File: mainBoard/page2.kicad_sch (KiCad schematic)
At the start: 4 parts, among them IC1 TCAN3414DR, J12 Conn_02x20_Odd_Even, J13 RJ45

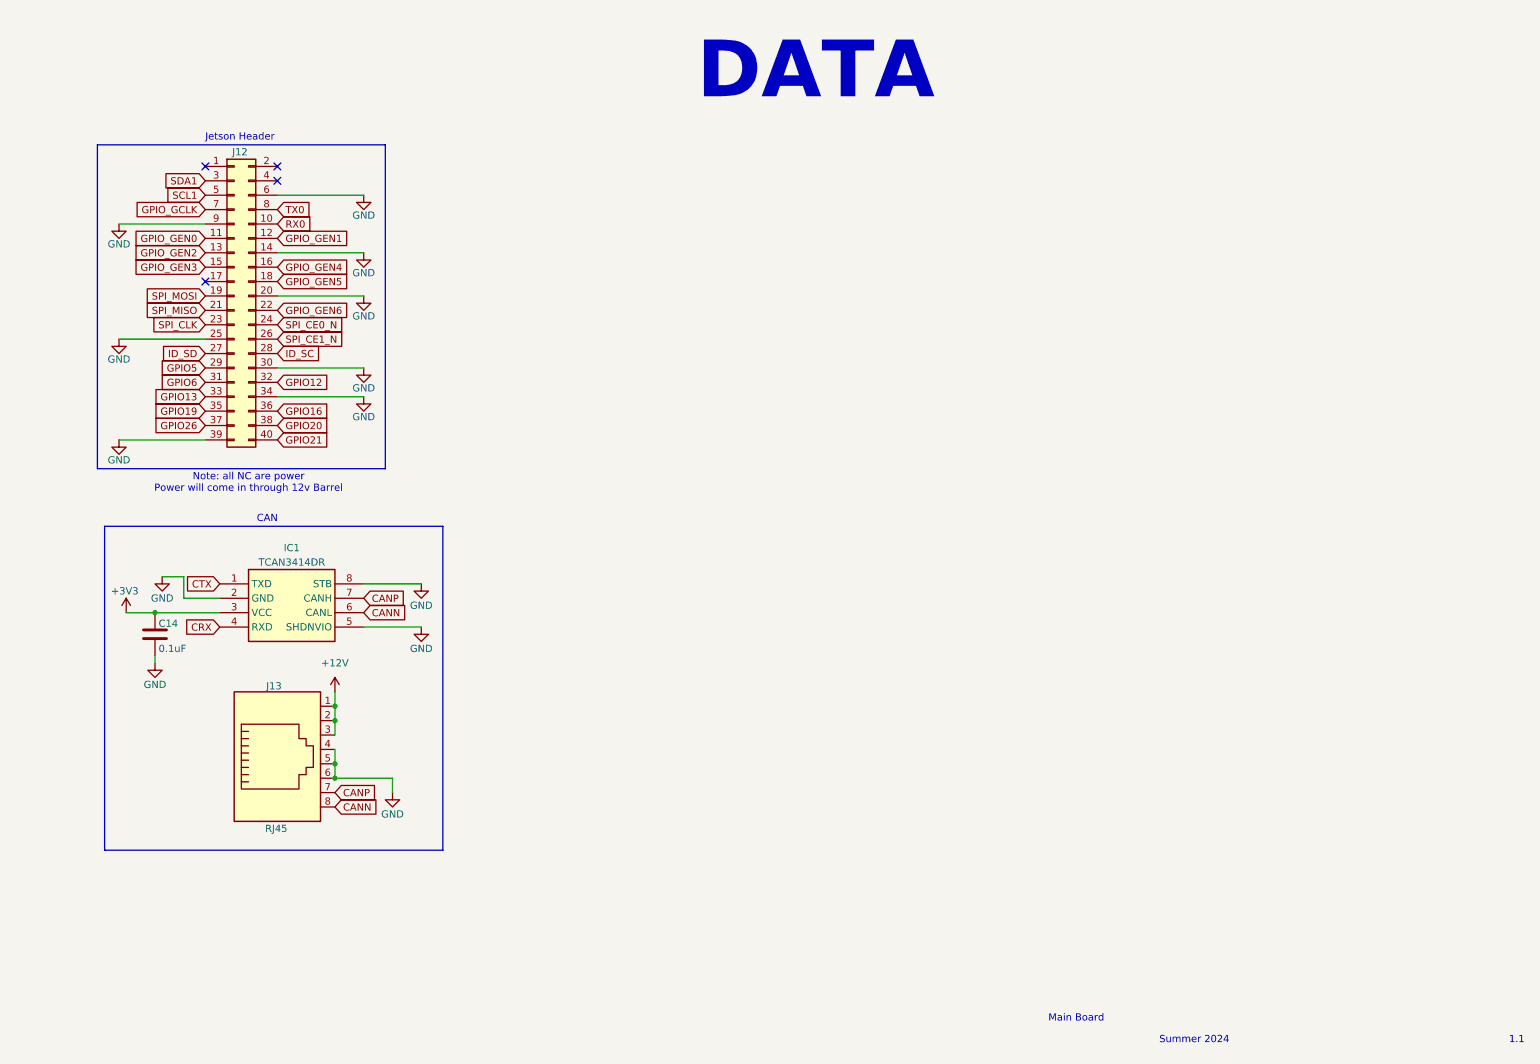
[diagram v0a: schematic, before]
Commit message: Added QWIIC Connectors for i2c, ethernet ports for attachment, updated XT style power connector counts, added i2c multiplexer
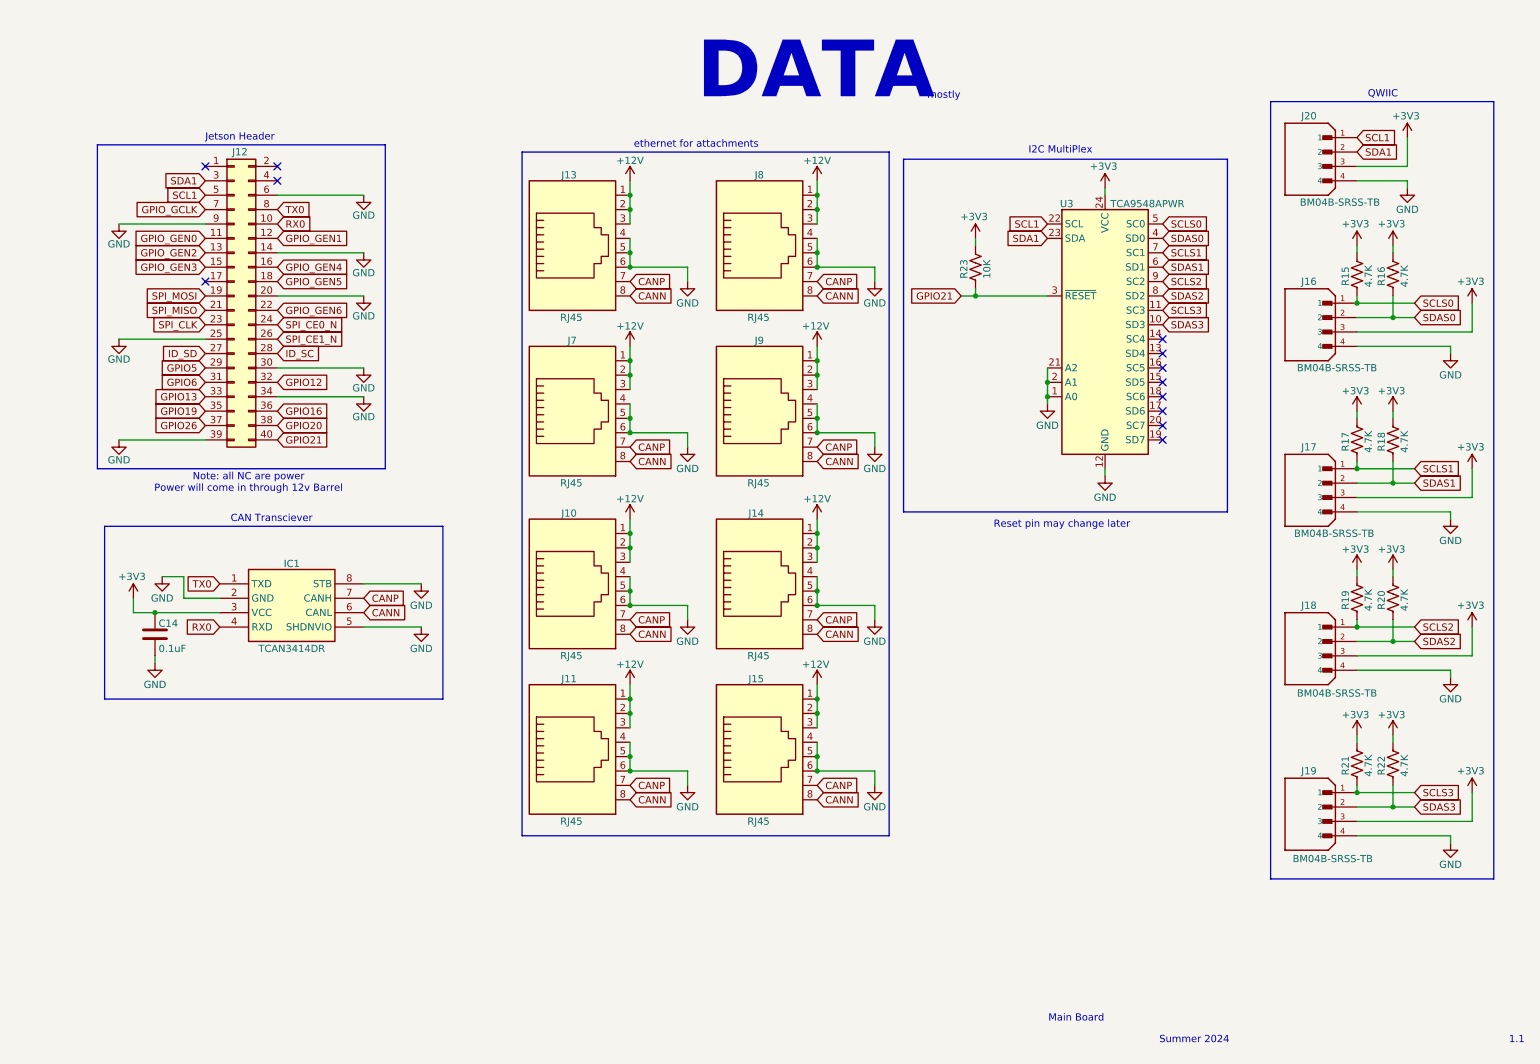
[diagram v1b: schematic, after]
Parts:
- added J10, J11, J14, J15, J7, J8, J9: RJ45, symbol Connector:RJ45
- added J16, J17, J18, J19, J20: BM04B-SRSS-TB, Connector_JST:JST_SH_BM04B-SRSS-TB_1x04-1MP_P1.00mm_Vertical, symbol QWIIC:PRT-14417
- added R15, R16, R17, R18, R19, R20, R21, R22: 4.7K, Resistor_SMD:R_0805_2012Metric_Pad1.20x1.40mm_HandSolder, symbol Device:R_US
- added R23: 10K, Resistor_SMD:R_0805_2012Metric_Pad1.20x1.40mm_HandSolder, symbol Device:R_US
- added U3: TCA9548APWR, Package_SO:TSSOP-24_4.4x7.8mm_P0.65mm, symbol Interface_Expansion:TCA9548APWR
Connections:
- net CRX is gone; now on net RX0: IC1.4 (RXD)
- net CTX is gone; now on net TX0: IC1.1 (TXD)
- net +12V: now also J10.1, J10.2, J10.3, J11.1, J11.2, J11.3, J14.1, J14.2, J14.3, J15.1, J15.2, J15.3, J7.1, J7.2, J7.3, J8.1, J8.2, J8.3, J9.1, J9.2, J9.3
- net +3V3: now also J16.3, J17.3, J18.3, J19.3, J20.3, R15.1, R16.1, R17.1, R18.1, R19.1, R20.1, R21.1, R22.1, R23.1, U3.24 (VCC)
- net CANN: now also J10.8, J11.8, J14.8, J15.8, J7.8, J8.8, J9.8
- net CANP: now also J10.7, J11.7, J14.7, J15.7, J7.7, J8.7, J9.7
- net GND: now also J10.4, J10.5, J10.6, J11.4, J11.5, J11.6, J14.4, J14.5, J14.6, J15.4, J15.5, J15.6, J16.4, J17.4, J18.4, J19.4, J20.4, J7.4, J7.5, J7.6, J8.4, J8.5, J8.6, J9.4, J9.5, J9.6, U3.1 (A0), U3.12 (GND), U3.2 (A1), U3.21 (A2)
- net GPIO21: now also R23.2, U3.3 (~{RESET})
- net SCL1: now also J20.1, U3.22 (SCL)
- net SDA1: now also J20.2, U3.23 (SDA)
- new net SCLS0: J16.1, R15.2, U3.5 (SC0)
- new net SCLS1: J17.1, R17.2, U3.7 (SC1)
- new net SCLS2: J18.1, R19.2, U3.9 (SC2)
- new net SCLS3: J19.1, R21.2, U3.11 (SC3)
- new net SDAS0: J16.2, R16.2, U3.4 (SD0)
- new net SDAS1: J17.2, R18.2, U3.6 (SD1)
- new net SDAS2: J18.2, R20.2, U3.8 (SD2)
- new net SDAS3: J19.2, R22.2, U3.10 (SD3)
- no-connect marks 4 -> 12
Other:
- note added: "CAN Transciever"
- note added: "I2C MultiPlex"
- note added: "QWIIC"
- note added: "Reset pin may change later"
- note added: "ethernet for attachments"
- note added: "mostly"
- note removed: "CAN"
- moved on the sheet: J13

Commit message: Minor changes, renamed ethernet ports to attachment and adding warning
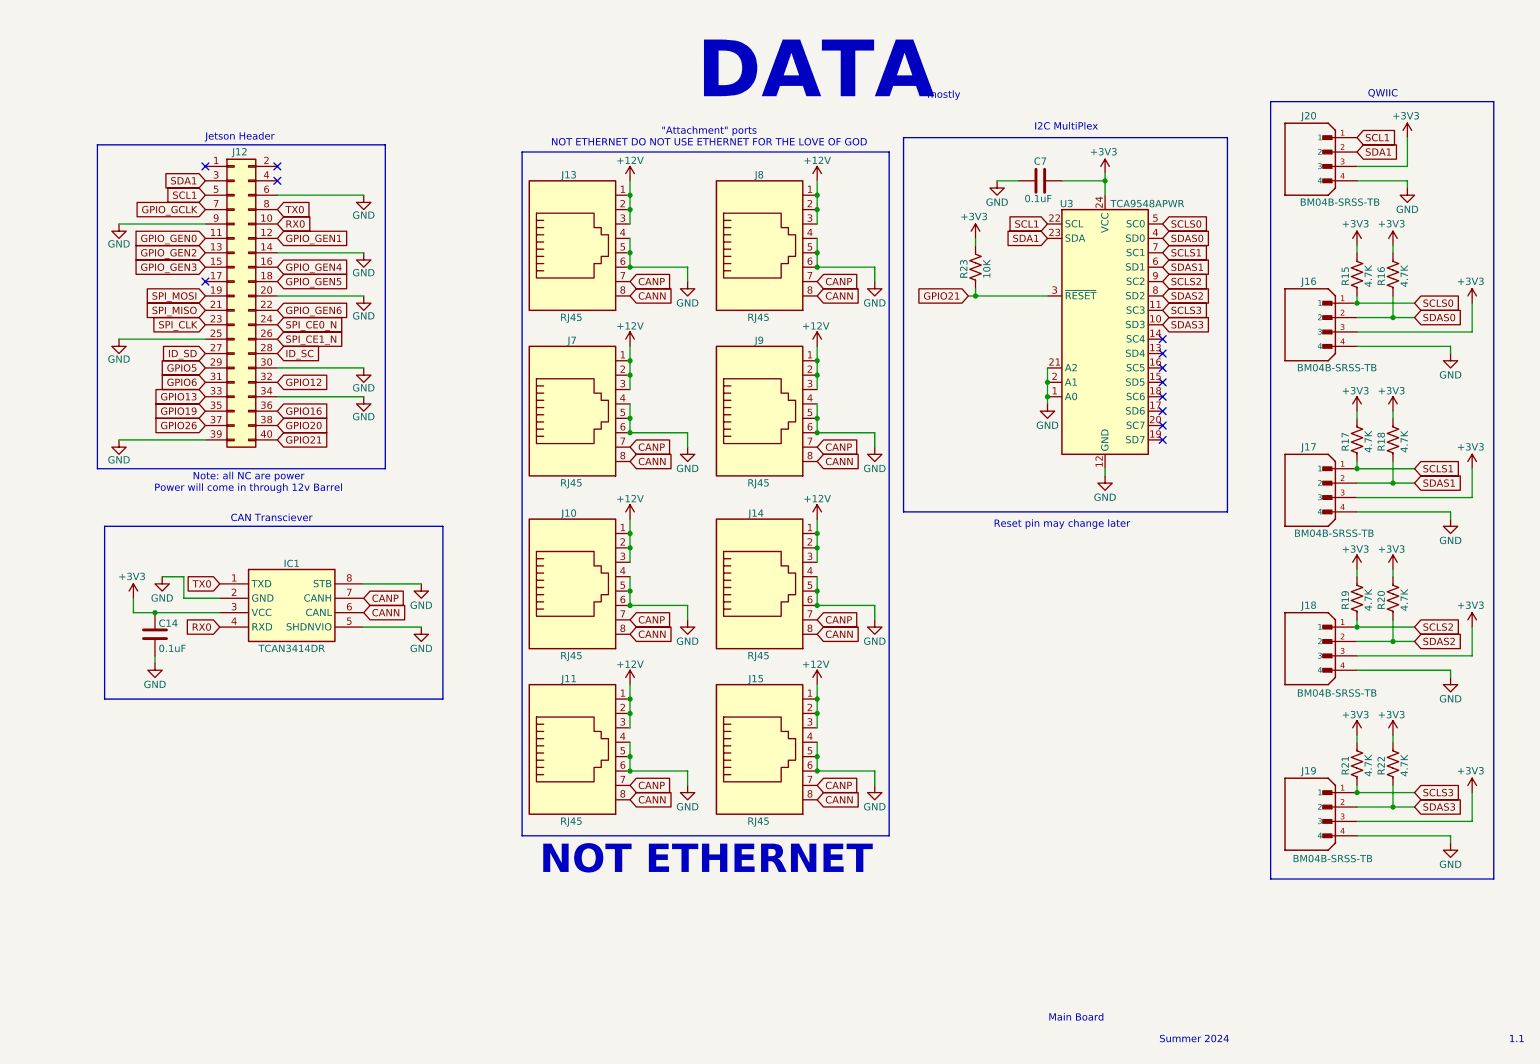
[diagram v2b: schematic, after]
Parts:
- added C7: 0.1uF, Capacitor_SMD:C_0805_2012Metric_Pad1.18x1.45mm_HandSolder, symbol Device:C
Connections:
- net +3V3: now also C7.1
- net GND: now also C7.2
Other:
- note added: ""Attachment" ports NOT ETHERNET DO NOT USE ETHERNET FOR THE LOVE OF GOD"
- note added: "NOT ETHERNET"
- note removed: "ethernet for attachments"
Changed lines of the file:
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@@
 	)
 	(junction
+		(at 196.85 41.91)
+		(diameter 0)
+		(color 0 0 0 0)
+	)
+	(junction
 		(at 146.05 133.35)
 		(diameter 0)
@@
 	(wire
 		(pts
-			(xy 196.85 43.18) (xy 196.85 44.45)
-		)
-		(stroke
-			(width 0)
-			(type default)
-		)
-	)
-	(wire
-		(pts
 			(xy 247.65 66.04) (xy 241.3 66.04)
 		)
@@
 	(wire
 		(pts
-			(xy 171.45 62.23) (xy 173.99 62.23)
+			(xy 172.72 62.23) (xy 173.99 62.23)
 		)
 		(stroke
@@
 	(wire
 		(pts
+			(xy 189.23 41.91) (xy 196.85 41.91)
+		)
+		(stroke
+			(width 0)
+			(type default)
+		)
+	)
+	(wire
+		(pts
 			(xy 261.62 63.5) (xy 261.62 68.58)
 		)
@@
 	(wire
 		(pts
+			(xy 196.85 41.91) (xy 196.85 44.45)
+		)
+		(stroke
+			(width 0)
+			(type default)
+		)
+	)
+	(wire
+		(pts
 			(xy 241.3 91.44) (xy 241.3 92.71)
 		)
@@
 	(wire
 		(pts
+			(xy 177.8 41.91) (xy 181.61 41.91)
+		)
+		(stroke
+			(width 0)
+			(type default)
+		)
+	)
+	(wire
+		(pts
 			(xy 34.29 111.76) (xy 34.29 115.57)
 		)
@@
 	(wire
 		(pts
+			(xy 196.85 40.64) (xy 196.85 41.91)
+		)
+		(stroke
+			(width 0)
+			(type default)
+		)
+	)
+	(wire
+		(pts
 			(xy 29.21 127) (xy 29.21 125.73)
 		)
@@
 	)
 	(rectangle
-		(start 161.29 38.1)
+		(start 161.29 34.29)
 		(end 218.44 100.33)
 		(stroke
@@
 		)
 	)
-	(text "ethernet for attachments"
+	(text "\"Attachment\" ports\nNOT ETHERNET DO NOT USE ETHERNET FOR THE LOVE OF GOD"
 		(exclude_from_sim no)
-		(at 124.714 35.56 0)
+		(at 127 34.29 0)
 		(effects
 			(font
@@
 	(text "I2C MultiPlex"
 		(exclude_from_sim no)
-		(at 188.976 36.576 0)
+		(at 189.992 32.512 0)
 		(effects
 			(font
@@
 		)
 	)
+	(text "NOT ETHERNET"
+		(exclude_from_sim no)
+		(at 126.492 161.798 0)
+		(effects
+			(font
+				(size 5 5)
+				(thickness 1)
+				(bold yes)
+			)
+		)
+	)
 	(text "Summer 2024"
 		(exclude_from_sim no)
@@
 	(global_label "GPIO21"
 		(shape input)
-		(at 171.45 62.23 180)
+		(at 172.72 62.23 180)
 		(fields_autoplaced yes)
 		(effects
@@
 		)
 		(property "Intersheetrefs" "${INTERSHEET_REFS}"
-			(at 162.2247 62.23 0)
+			(at 163.4947 62.23 0)
 			(effects
 				(font
@@
 	)
 	(symbol
+		(lib_id "Device:C")
+		(at 185.42 41.91 270)
+		(unit 1)
+		(exclude_from_sim no)
+		(in_bom yes)
+		(on_board yes)
+		(dnp no)
+		(property "Reference" "C7"
+			(at 184.2771 38.481 90)
+			(effects
+				(font
+					(size 1.27 1.27)
+				)
+				(justify left)
+			)
+		)
+		(property "Value" "0.1uF"
+			(at 182.6261 45.085 90)
+			(effects
+				(font
+					(size 1.27 1.27)
+				)
+				(justify left)
+			)
+		)
+		(property "Footprint" "Capacitor_SMD:C_0805_2012Metric_Pad1.18x1.45mm_HandSolder"
+			(at 181.61 42.8752 0)
+			(effects
+				(font
+					(size 1.27 1.27)
+				)
+				(hide yes)
+			)
+		)
+		(property "Datasheet" "~"
+			(at 185.42 41.91 0)
+			(effects
+				(font
+					(size 1.27 1.27)
+				)
+				(hide yes)
+			)
+		)
+		(property "Description" "Unpolarized capacitor"
+			(at 185.42 41.91 0)
+			(effects
+				(font
+					(size 1.27 1.27)
+				)
+				(hide yes)
+			)
+		)
+		(pin "1"
+		)
+		(pin "2"
+		)
+		(instances
+			(project "mainBoard"
+				(path "/c4a17c19-34f8-41cd-9019-636b61180dc7/bb7cdc9a-56be-4d98-b438-561aac97a030"
+					(reference "C7")
+					(unit 1)
+				)
+			)
+		)
+	)
+	(symbol
 		(lib_id "power:+12V")
 		(at 113.03 71.12 0)
@@
 	(symbol
 		(lib_id "power:+3V3")
-		(at 196.85 43.18 0)
+		(at 196.85 40.64 0)
 		(unit 1)
 		(exclude_from_sim no)
@@
 		(dnp no)
 		(property "Reference" "#PWR068"
-			(at 196.85 46.99 0)
+			(at 196.85 44.45 0)
 			(effects
 				(font
@@
 		)
 		(property "Value" "+3V3"
-			(at 196.596 39.37 0)
+			(at 196.596 36.83 0)
 			(effects
 				(font
@@
 		)
 		(property "Footprint" ""
-			(at 196.85 43.18 0)
+			(at 196.85 40.64 0)
 			(effects
 				(font
@@
 		)
 		(property "Datasheet" ""
-			(at 196.85 43.18 0)
+			(at 196.85 40.64 0)
 			(effects
 				(font
@@
 		)
 		(property "Description" "Power symbol creates a global label with name \"+3V3\""
-			(at 196.85 43.18 0)
+			(at 196.85 40.64 0)
 			(effects
 				(font
@@
 					(unit 1)
 				)
+			)
+		)
+	)
+	(symbol
+		(lib_id "power:GND")
+		(at 177.8 41.91 0)
+		(unit 1)
+		(exclude_from_sim no)
+		(in_bom yes)
+		(on_board yes)
+		(dnp no)
+		(property "Reference" "#PWR089"
+			(at 177.8 48.26 0)
+			(effects
+				(font
+					(size 1.27 1.27)
+				)
+				(hide yes)
+			)
+		)
+		(property "Value" "GND"
+			(at 177.8 45.72 0)
+			(effects
+				(font
+					(size 1.27 1.27)
+				)
+			)
+		)
+		(property "Footprint" ""
+			(at 177.8 41.91 0)
+			(effects
+				(font
+					(size 1.27 1.27)
+				)
+				(hide yes)
+			)
+		)
+		(property "Datasheet" ""
+			(at 177.8 41.91 0)
+			(effects
+				(font
+					(size 1.27 1.27)
+				)
+				(hide yes)
+			)
+		)
+		(property "Description" "Power symbol creates a global label with name \"GND\" , ground"
+			(at 177.8 41.91 0)
+			(effects
+				(font
+					(size 1.27 1.27)
+				)
+				(hide yes)
+			)
+		)
+		(pin "1"
+		)
+		(instances
+			(project "mainBoard"
+				(path "/c4a17c19-34f8-41cd-9019-636b61180dc7/bb7cdc9a-56be-4d98-b438-561aac97a030"
+					(reference "#PWR089")
+					(unit 1)
+				)

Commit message: Started laying out the board
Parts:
- added R3: 120, Resistor_SMD:R_0805_2012Metric_Pad1.20x1.40mm_HandSolder, symbol Device:R_US
- IC1: footprint SOIC127P600X175-8N -> footprints:SOIC127P600X175-8N
- J10, J11, J13, J14, J15, J7, J8, J9: footprint (none) -> Connector_RJ:RJ45_Amphenol_54602-x08_Horizontal
- J16, J17, J18, J19, J20: value BM04B-SRSS-TB -> BM04B-SRSS-TB
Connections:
- net CANN: now also R3.2
- net CANP: now also R3.1
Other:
- note added: "PLEASE UNDERSTAND THESE ARE NOT ETHERNET DO NOT PLUG INTO JETSON"
- note added: "maybe add a terminating resistor to match impedance?"
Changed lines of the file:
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@@
 	(rectangle
 		(start 20.32 102.87)
-		(end 80.01 133.35)
+		(end 90.17 133.35)
 		(stroke
 			(width 0)
@@
 		)
 	)
+	(text "maybe add a terminating resistor\nto match impedance?"
+		(exclude_from_sim no)
+		(at 51.562 139.7 0)
+		(effects
+			(font
+				(size 3 3)
+				(thickness 0.6)
+				(bold yes)
+			)
+		)
+	)
 	(text "Note: all NC are power\nPower will come in through 12v Barrel"
 		(exclude_from_sim no)
@@
 		)
 	)
+	(text "PLEASE UNDERSTAND\nTHESE ARE NOT ETHERNET\nDO NOT PLUG INTO JETSON"
+		(exclude_from_sim no)
+		(at 123.952 182.626 0)
+		(effects
+			(font
+				(size 5 5)
+				(thickness 1)
+				(bold yes)
+			)
+		)
+	)
 	(text "QWIIC"
 		(exclude_from_sim no)
@@
 		)
 	)
+	(global_label "CANN"
+		(shape input)
+		(at 82.55 120.65 270)
+		(fields_autoplaced yes)
+		(effects
+			(font
+				(size 1.27 1.27)
+			)
+			(justify right)
+		)
+		(property "Intersheetrefs" "${INTERSHEET_REFS}"
+			(at 82.55 128.0006 90)
+			(effects
+				(font
+					(size 1.27 1.27)
+				)
+				(justify right)
+				(hide yes)
+			)
+		)
+	)
 	(global_label "SCLS0"
 		(shape input)
@@
 		)
 	)
+	(global_label "CANP"
+		(shape input)
+		(at 82.55 113.03 90)
+		(fields_autoplaced yes)
+		(effects
+			(font
+				(size 1.27 1.27)
+			)
+			(justify left)
+		)
+		(property "Intersheetrefs" "${INTERSHEET_REFS}"
+			(at 82.55 105.7399 90)
+			(effects
+				(font
+					(size 1.27 1.27)
+				)
+				(justify left)
+				(hide yes)
+			)
+		)
+	)
 	(global_label "SDAS0"
 		(shape input)
@@
 			)
 		)
-		(property "Footprint" ""
+		(property "Footprint" "Connector_RJ:RJ45_Amphenol_54602-x08_Horizontal"
 			(at 135.89 52.705 90)
 			(effects
@@
 			)
 		)
-		(property "Footprint" ""
+		(property "Footprint" "Connector_RJ:RJ45_Amphenol_54602-x08_Horizontal"
 			(at 102.87 112.395 90)
 			(effects
@@
 			)
 		)
-		(property "Value" " BM04B-SRSS-TB "
+		(property "Value" "BM04B-SRSS-TB"
 			(at 244.094 161.5439 0)
 			(effects
@@
 	)
 	(symbol
+		(lib_id "Device:R_US")
+		(at 82.55 116.84 0)
+		(unit 1)
+		(exclude_from_sim no)
+		(in_bom yes)
+		(on_board yes)
+		(dnp yes)
+		(property "Reference" "R3"
+			(at 80.518 118.8719 90)
+			(effects
+				(font
+					(size 1.27 1.27)
+				)
+				(justify left)
+			)
+		)
+		(property "Value" "120"
+			(at 84.582 118.8719 90)
+			(effects
+				(font
+					(size 1.27 1.27)
+				)
+				(justify left)
+			)
+		)
+		(property "Footprint" "Resistor_SMD:R_0805_2012Metric_Pad1.20x1.40mm_HandSolder"
+			(at 83.566 117.094 90)
+			(effects
+				(font
+					(size 1.27 1.27)
+				)
+				(hide yes)
+			)
+		)
+		(property "Datasheet" "~"
+			(at 82.55 116.84 0)
+			(effects
+				(font
+					(size 1.27 1.27)
+				)
+				(hide yes)
+			)
+		)
+		(property "Description" "Resistor, US symbol"
+			(at 82.55 116.84 0)
+			(effects
+				(font
+					(size 1.27 1.27)
+				)
+				(hide yes)
+			)
+		)
+		(pin "1"
+		)
+		(pin "2"
+		)
+		(instances
+			(project "mainBoard"
+				(path "/c4a17c19-34f8-41cd-9019-636b61180dc7/bb7cdc9a-56be-4d98-b438-561aac97a030"
+					(reference "R3")
+					(unit 1)
+				)
+			)
+		)
+	)
+	(symbol
 		(lib_id "power:GND")
 		(at 22.86 49.53 0)
@@
 			)
 		)
-		(property "Footprint" ""
+		(property "Footprint" "Connector_RJ:RJ45_Amphenol_54602-x08_Horizontal"
 			(at 135.89 81.915 90)
 			(effects
@@
 			)
 		)
-		(property "Footprint" ""
+		(property "Footprint" "Connector_RJ:RJ45_Amphenol_54602-x08_Horizontal"
 			(at 135.89 141.605 90)
 			(effects
@@
 			)
 		)
-		(property "Footprint" ""
+		(property "Footprint" "Connector_RJ:RJ45_Amphenol_54602-x08_Horizontal"
 			(at 102.87 141.605 90)
 			(effects
@@
 			)
 		)
-		(property "Footprint" ""
+		(property "Footprint" "Connector_RJ:RJ45_Amphenol_54602-x08_Horizontal"
 			(at 135.89 112.395 90)
 			(effects
@@
 			)
 		)
-		(property "Value" " BM04B-SRSS-TB "
+		(property "Value" "BM04B-SRSS-TB"
 			(at 245.364 45.7199 0)
 			(effects
@@
 			)
 		)
-		(property "Footprint" ""
+		(property "Footprint" "Connector_RJ:RJ45_Amphenol_54602-x08_Horizontal"
 			(at 102.87 81.915 90)
 			(effects
@@
 			)
 		)
-		(property "Value" " BM04B-SRSS-TB "
+		(property "Value" "BM04B-SRSS-TB"
 			(at 244.856 132.3339 0)
 			(effects
@@
 			)
 		)
-		(property "Value" " BM04B-SRSS-TB "
+		(property "Value" "BM04B-SRSS-TB"
 			(at 244.856 74.9299 0)
 			(effects
@@
 			)
 		)
-		(property "Footprint" ""
+		(property "Footprint" "Connector_RJ:RJ45_Amphenol_54602-x08_Horizontal"
 			(at 102.87 52.705 90)
 			(effects
@@
 			)
 		)
-		(property "Footprint" "SOIC127P600X175-8N"
+		(property "Footprint" "footprints:SOIC127P600X175-8N"
 			(at 69.85 207.95 0)
 			(effects
@@
 			)
 		)
-		(property "Value" " BM04B-SRSS-TB "
+		(property "Value" "BM04B-SRSS-TB"
 			(at 244.348 104.1399 0)
 			(effects
